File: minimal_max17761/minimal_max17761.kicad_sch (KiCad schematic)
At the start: 20 parts, among them U1 MAX17761ATC+

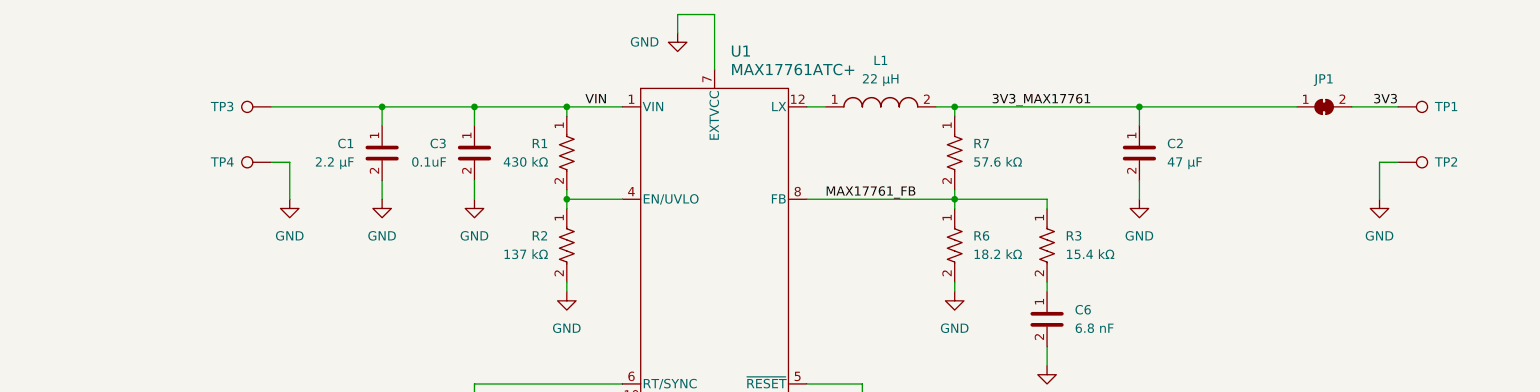
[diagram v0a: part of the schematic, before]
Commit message: Update minimal_max17761.pdf with formatting adjustments and additional details
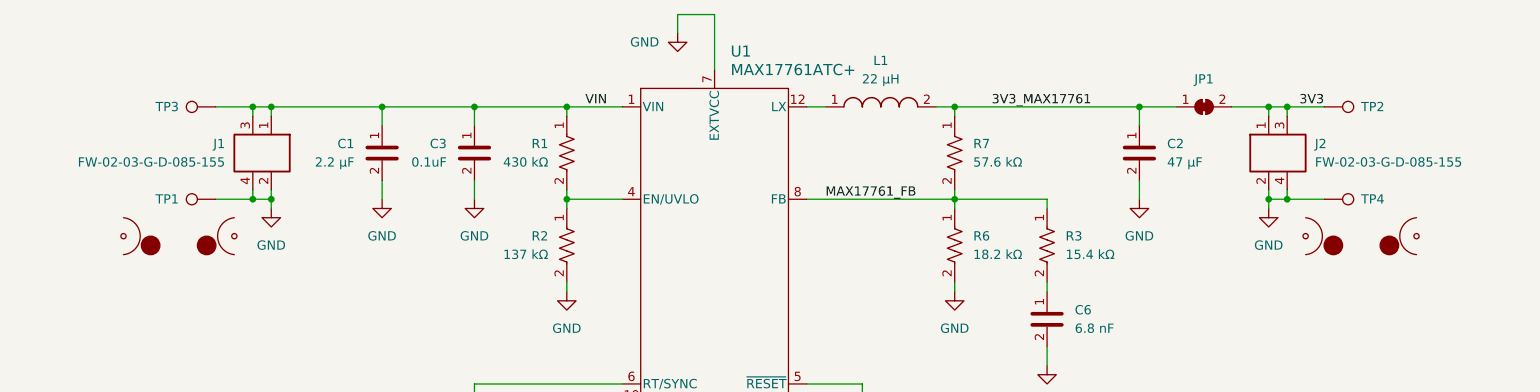
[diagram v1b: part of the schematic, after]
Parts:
- added J1, J2: FW-02-03-G-D-085-155, connector_footprints:FW-02-03-G-D-085-155, symbol UNITED_CONNECTORS_DATA_BASE:J_FW-02-03-G-D-085-155
- added MB1, MB2: mouse-bite-midle-50mil-200mil, mouse_bite_footprints:mouse-bite-midle-50mil-200mil, symbol UNITED_MOUSE_BITES_DATA_BASE:mouse-bite-midle-50mil-200mil
- renumbered TP4 to TP1, TP1 to TP2, TP2 to TP4
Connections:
- net 3V3: now also J2.1, J2.3
- net GND: now also J1.2, J1.4, J2.2, J2.4
- net VIN: now also J1.1, J1.3
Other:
- moved on the sheet: JP1, TP1, TP2, TP3, TP4

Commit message: Update footprint library URIs to use KiCAD_Symbols_Generator
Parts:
- C3, C5: value 0.1uF -> 100 nF; 3dviewer Link (none) -> https://3dviewer.net/index.html#model=https://github.com/io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; Capacitor Type (none) -> Ceramic
- R4: value 10k -> 10 kΩ; 3dviewer Link (none) -> https://3dviewer.net/index.html#model=https://github.com/io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; Component Type (none) -> Resistor
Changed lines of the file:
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@@
 			)
 		)
-		(property "Value" "10k"
+		(property "Value" "10 kΩ"
 			(at 175.26 124.4599 90)
 			(effects
@@
 			)
 		)
+		(property "3dviewer Link" "https://3dviewer.net/index.html#model=https://github.com/ionutms/KiCAD_Symbols_Generator/blob/main/3D_models/R_0402.step"
+			(at 160.02 123.19 0)
+			(effects
+				(font
+					(size 1.27 1.27)
+				)
+				(justify left)
+				(hide yes)
+			)
+		)
+		(property "Component Type" "Resistor"
+			(at 152.4 123.19 0)
+			(effects
+				(font
+					(size 1.27 1.27)
+				)
+				(justify left)
+				(hide yes)
+			)
+		)
 		(pin "1"
 		)
@@
 			)
 		)
-		(property "Value" "0.1uF"
+		(property "Value" "100 nF"
 			(at 115.57 86.3599 90)
 			(effects
@@
 			)
 		)
+		(property "3dviewer Link" "https://3dviewer.net/index.html#model=https://github.com/ionutms/KiCAD_Symbols_Generator/blob/main/3D_models/C_0402.step"
+			(at 104.14 85.09 0)
+			(effects
+				(font
+					(size 1.27 1.27)
+				)
+				(justify left)
+				(hide yes)
+			)
+		)
+		(property "Capacitor Type" "Ceramic"
+			(at 101.6 85.09 0)
+			(effects
+				(font
+					(size 1.27 1.27)
+				)
+				(justify left)
+				(hide yes)
+			)
+		)
 		(pin "2"
 		)
@@
 			)
 		)
-		(property "Value" "0.1uF"
+		(property "Value" "100 nF"
 			(at 128.27 137.1599 90)
 			(effects
@@
 			(effects
 				(font
+					(size 1.27 1.27)
+				)
+				(justify left)
+				(hide yes)
+			)
+		)
+		(property "3dviewer Link" "https://3dviewer.net/index.html#model=https://github.com/ionutms/KiCAD_Symbols_Generator/blob/main/3D_models/C_0402.step"
+			(at 116.84 135.89 0)
+			(effects
+				(font
+					(size 1.27 1.27)
+				)
+				(justify left)
+				(hide yes)
+			)
+		)
+		(property "Capacitor Type" "Ceramic"
+			(at 114.3 135.89 0)
+			(effects
+				(font

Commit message: Switch to KiCad 9
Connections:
- net ~{RESET}: now reaches R4.1, U1.5 (~{RESET})
- net VCC: now reaches C4.1, R4.2, U1.3 (VCC)
- net EN/UVLO: now reaches R1.2, R2.1, U1.4 (EN/UVLO)
- net RT/SYNC: now reaches R5.1, U1.6 (RT/SYNC)
- net SS: now reaches C5.1, U1.9 (SS)
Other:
- moved on the sheet: C1, C3, J1, R1, R2, TP1, TP3

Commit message: Backup
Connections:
- net LX: now reaches L1.1, U1.12 (LX)
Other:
- moved on the sheet: C1, C2, C3, C4, C5, C6, J1, J2, JP1, L1, R1, R2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
